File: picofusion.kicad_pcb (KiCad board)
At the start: 4 copper layers, 25.5 x 25.5 mm, 102 parts, among them J1 NORTH, J2 EAST, J3 WEST, J4 SOUTH, U1 W25Q16, U2 RP2040, U3 TLV71333PDQN, U4 ICM42605, U5 MMC5983MA, U6 ICP20100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

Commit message: draft: schematic and layout for H20R1
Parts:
- removed C13, C15, C24, C26: 0.1uF, Capacitor_SMD:C_0201_0603Metric
- removed C25: 1uF, Capacitor_SMD:C_0201_0603Metric
- removed R2, R3: 27, Resistor_SMD:R_0201_0603Metric
- removed R4, R5: 10K, Resistor_SMD:R_0402_1005Metric
- removed U2: RP2040, RP2040_minimal:RP2040-QFN-56
- C1: value 0.1uF -> 2u2
- C10: value 0.1uF -> 1u0
- C2, C4, C7, C9: value 0.1uF -> 0u1
- C3: value 1uF -> 0u1
- C6: value 0.1uF -> 4u7
- TP1: moved to F.Cu
- U1: value W25Q16 -> STM32F412CGUx; footprint USON:8-USON -> Package_DFN_QFN:QFN-48-1EP_7x7mm_P0.5mm_EP5.6x5.6mm
- moved C17 13.6 mm to (168.5, 39.2)
- moved C18 13.6 mm to (169.8, 37.6)
- moved C19 13.6 mm to (166.4, 39.2)
- moved U4 13.6 mm to (167.5, 37.1)
- moved C10 12.6 mm to (164.2, 50.0), turned to 180 degrees
- moved R14 12.6 mm to (158.6, 38.6), turned to -90 degrees
- moved C29 10.0 mm to (155.9, 40.8)
- moved C30 10.0 mm to (157.1, 39.5)
- moved U8 10.0 mm to (157.1, 40.8)
- moved C23 8.57 mm to (153.9, 36.9)
- moved C22 8.57 mm to (155.7, 38.7)
- moved U6 8.57 mm to (153.9, 38.7)
- moved R17 8.53 mm to (169.2, 45.4), turned to 180 degrees
- moved U1 7.93 mm to (163.0, 43.9)
- moved C1 7.65 mm to (168.0, 42.1), turned to 180 degrees
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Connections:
- C1 pad 1: +1V1 -> GND
- C1 pad 2: GND -> Net-(C1-Pad2)
- C11 pad 1: /RUN -> /nRST
- C2 pad 1: +1V1 -> +3V3
- C3 pad 1: +1V1 -> +3V3
- J1 pad 4: /I2C0_SCL -> /I2C1_SCL
- J1 pad 5: /I2C0_SDA -> /I2C1_SDA
- J2 pad 1: /SPI1_SCK_SD -> /SDIO_CMD
- J2 pad 2: /SPI1_POCI_SD -> /SDIO_D3
- J2 pad 3: /SPI1_PICO_SD -> /SDIO_D2
- J2 pad 4: /SPI1_nCS_SD -> /SDIO_D1
- J2 pad 5: /SD_nCD -> /SDIO_D0
- J2 pad 9: /RUN -> /nRST
- J4 pad 4: /UART0_TX_TELEM -> /UART2_TX_TELEM
- J4 pad 5: /UART0_RX_TELEM -> /UART2_RX_TELEM
- J4 pad 6: /UART0_CTS_TELEM -> /UART2_CTS_TELEM
- J4 pad 7: /UART0_RTS_TELEM -> /UART2_RTS_TELEM
- R1 pad 2: /RUN -> /nRST
- R12 pad 1: /PIO0_CAN_TX -> /CAN1_TX
- R13 pad 1: /PIO0_CAN_RX -> /CAN1_RX
- R18 pad 1: /RUN -> /nRST
- R8 pad 2: /I2C0_SCL -> /I2C1_SCL
- R9 pad 2: /I2C0_SDA -> /I2C1_SDA
- U1 pad 1: /QSPI_nCS -> +3V3
- U1 pad 2: /QSPI_SD1 -> unconnected-(U1-Pad2)
- U1 pad 3: /QSPI_SD2 -> /CAN_SILENT
- U1 pad 4: GND -> /IMU_HEATER
- U1 pad 5: /QSPI_SD0 -> /XIN
- U1 pad 6: /QSPI_SCK -> /XOUT
- U1 pad 7: /QSPI_SD3 -> /nRST
- U1 pad 8: +3V3 -> GND
- U5 pad 1: /I2C0_SCL -> /I2C1_SCL
- U5 pad 16: /I2C0_SDA -> /I2C1_SDA
- U6 pad 2: /I2C0_SCL -> /I2C1_SCL
- U6 pad 4: /I2C0_SDA -> /I2C1_SDA
- U7 pad 1: /PIO0_CAN_TX -> /CAN1_TX
- U7 pad 4: /PIO0_CAN_RX -> /CAN1_RX
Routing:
- net +5V: track 49.8 -> 14.9 mm, vias 6 -> 3
- net /I2C0_SCL: track 32.3 -> 0.00 mm, vias 3 -> 0
- net /I2C0_SDA: track 30.6 -> 0.00 mm, vias 2 -> 0
- net /I2C1_SCL: track 0.00 -> 27.2 mm, vias 0 -> 3
- net /I2C1_SDA: track 0.00 -> 26.2 mm, vias 0 -> 2
- net /RESV1: track 23.2 -> 0.00 mm, vias 1 -> 0
- net /SDIO_D3: track 0.00 -> 23.0 mm, vias 0 -> 1
- net /QSPI_nCS: track 23.1 -> 2.66 mm, vias 2 -> 0
- net /SDIO_D0: track 0.00 -> 20.3 mm, vias 0 -> 1
- net /SDIO_CMD: track 0.00 -> 18.2 mm
- net /BOOTSEL: track 3.94 -> 21.2 mm, vias 0 -> 4
- net +1V1: track 16.3 -> 0.00 mm, vias 2 -> 0
- net Net-(D4-Pad3): track 23.3 -> 7.92 mm, vias 4 -> 2
- net /SPI0_POCI: track 20.2 -> 5.32 mm
- net /UART0_TX_TELEM: track 14.7 -> 0.00 mm
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
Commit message: h20r1: more updates
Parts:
- moved C5 4.13 mm to (154.9, 49.1)
- moved C8 3.23 mm to (159.7, 50.6), turned to 0 degrees
- moved C2 2.68 mm to (157.9, 47.4), turned to 180 degrees
- moved G*** 2.29 mm to (162.7, 32.5)
- moved Y1 1.34 mm to (157.1, 49.9), turned to -90 degrees
- moved C10 0.68 mm to (163.6, 49.8)
- moved C9 0.68 mm to (163.6, 49.0)
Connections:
- U1 pad 2: unconnected-(U1-Pad2) -> /CAN_SILENT
- U1 pad 3: /CAN_SILENT -> /IMU_HEATER
- U1 pad 4: /IMU_HEATER -> unconnected-(U1-Pad4)
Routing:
- net /I2C1_SCL: track 27.2 -> 30.4 mm, vias 3 -> 2
- net /XOUT: track 9.60 -> 6.86 mm
- net /XIN: track 7.00 -> 9.71 mm
- net /UART2_RTS_TELEM: track 8.00 -> 6.62 mm, vias 1 -> 0
- net +3V3: track 33.5 -> 34.7 mm, vias 24 -> 23
- net /BOOTSEL: track 21.2 -> 20.1 mm, vias 4 -> 2
- net /CAN_SILENT: track 13.1 -> 12.2 mm, vias 2 -> 0
- net /IMU_HEATER: track 13.1 -> 12.3 mm
- net GND: track 36.1 -> 36.9 mm, vias 42 -> 43
- net /nRST: track 11.3 -> 11.9 mm, vias 2 -> 4
- net /UART2_RX_TELEM: track 13.0 -> 12.8 mm, vias 0 -> 1
- net /UART2_TX_TELEM: track 13.3 -> 13.4 mm, vias 0 -> 1
- net /UART2_CTS_TELEM: track 8.04 -> 8.12 mm, vias 1 -> 0

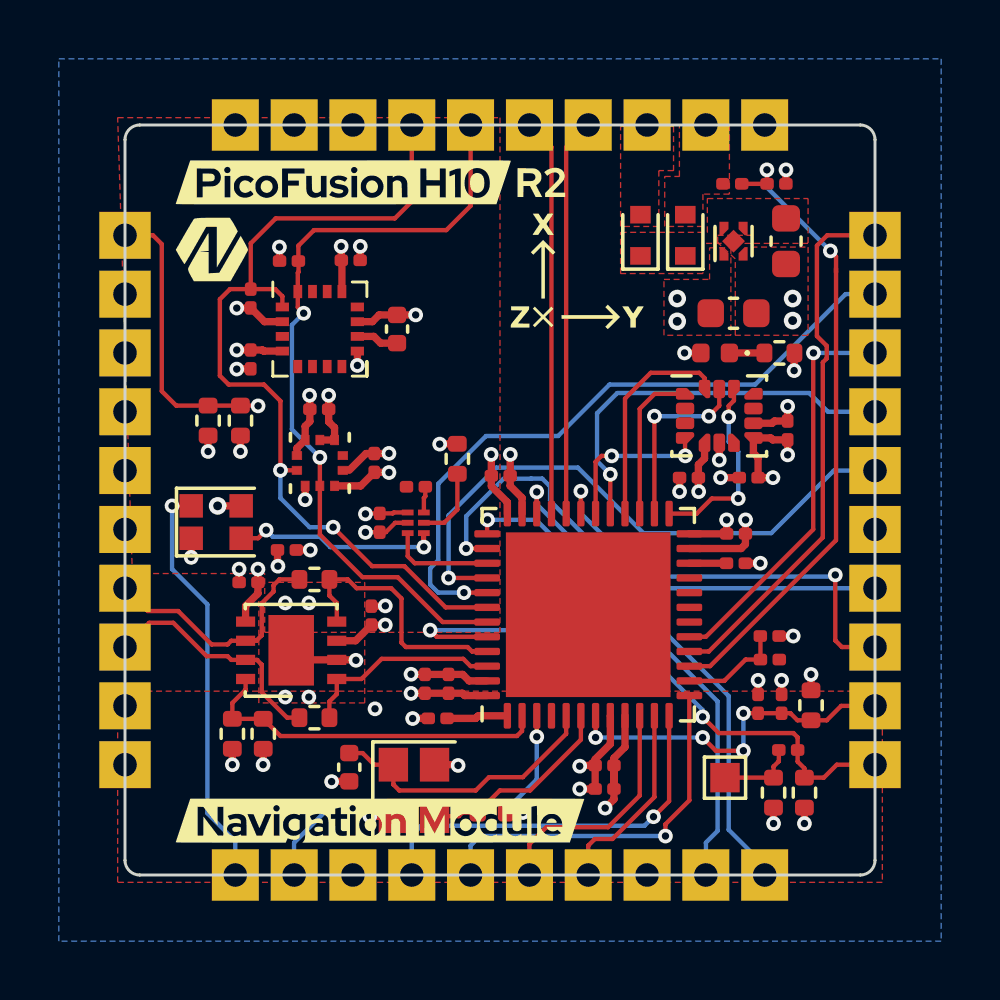
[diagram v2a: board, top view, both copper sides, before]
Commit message: replace sdio with spi2, finish routing, front silkscreen
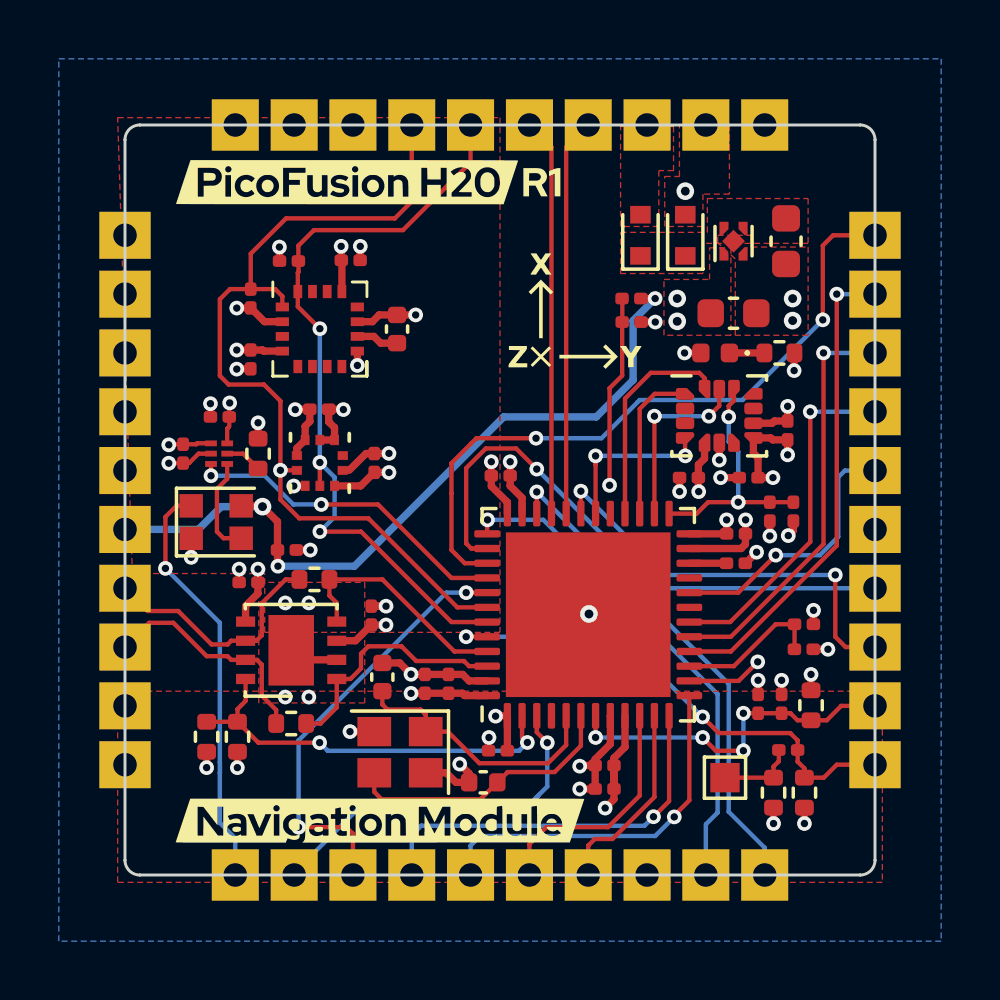
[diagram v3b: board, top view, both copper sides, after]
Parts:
- removed the G*** at (154.7, 29.2)
- removed the G*** at (150.2, 31.5)
- removed the G*** at (170.5, 29.2)
- added G***: LOGO, picofusion_stamp:r1, F.Cu at (162.3, 29.2)
- added G***: LOGO, picofusion_stamp:picofusion-h20, F.Cu at (155.9, 29.2)
- R23, R7: footprint Resistor_SMD:R_0402_1005Metric -> Resistor_SMD:R_0201_0603Metric
- moved R23 19.3 mm to (169.2, 40.4)
- moved R7 19.1 mm to (170.0, 40.4)
- moved R15 16.0 mm to (170.3, 45.1), turned to 180 degrees
- moved R16 15.0 mm to (170.3, 44.2)
- moved R17 13.1 mm to (164.5, 33.1)
- moved R22 11.7 mm to (164.5, 34.0)
- moved U8 7.09 mm to (150.4, 38.4)
- moved C29 7.09 mm to (149.2, 38.4)
- moved C30 7.08 mm to (150.5, 37.2)
- moved R14 6.78 mm to (151.8, 38.4)
- moved C5 3.26 mm to (156.0, 46.0), turned to 90 degrees
- moved C2 2.33 mm to (159.9, 48.5)
- moved Y1 1.38 mm to (156.6, 48.6), turned to 180 degrees
- moved G*** 1.35 mm to (162.6, 33.9)
- moved C8 1.07 mm to (159.4, 49.6), turned to 180 degrees
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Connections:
- net /SDIO_D2 renamed /SPI1_PICO
- J1 pad 3: /RESV1 -> unconnected-(J1-Pin_3-Pad3)
- J2 pad 1: /SDIO_CMD -> /SPI1_SCK
- J2 pad 2: /SDIO_D3 -> /SPI1_POCI
- J2 pad 4: /SDIO_D1 -> /SPI1_nCS
- J2 pad 5: /SDIO_D0 -> /RESV1
- J3 pad 1: /SPI0_nCS -> unconnected-(J3-Pin_1-Pad1)
- J3 pad 2: /SPI0_SCK -> unconnected-(J3-Pin_2-Pad2)
- J3 pad 3: /SPI0_PICO -> unconnected-(J3-Pin_3-Pad3)
- J3 pad 4: /SPI0_POCI -> unconnected-(J3-Pin_4-Pad4)
- J3 pad 5: /DRDY_ICM42605 -> unconnected-(J3-Pin_5-Pad5)
- U1 pad 16: /SDIO_CMD -> /SPI1_POCI
- U1 pad 18: /BUZZER -> /SPI1_nCS
- U1 pad 19: /RESV1 -> unconnected-(U1-PB1-Pad19)
- U1 pad 20: unconnected-(U1-Pad20) -> /RESV1
- U1 pad 29: /SDIO_D1 -> unconnected-(U1-PA8-Pad29)
- U1 pad 39: /NEOPIXEL_3V3 -> /SPI1_SCK
- U1 pad 40: /SDIO_D0 -> /NEOPIXEL_3V3
- U1 pad 41: /SDIO_D3 -> /BUZZER
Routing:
- net +5V: track 14.9 -> 41.9 mm, vias 3 -> 6
- net /SPI1_SCK: track 0.00 -> 23.4 mm, vias 0 -> 2
- net /SDIO_D3: track 23.0 -> 0.00 mm, vias 1 -> 0
- net /SDIO_D0: track 20.3 -> 0.00 mm, vias 1 -> 0
- net /SDIO_CMD: track 18.3 -> 0.00 mm
- net /3V3_SENSE: track 21.8 -> 5.02 mm, vias 2 -> 0
- net /SPI1_POCI: track 0.00 -> 16.3 mm, vias 0 -> 1
- net /BUZZER: track 0.00 -> 14.7 mm, vias 0 -> 2
- net /5V_SENSE: track 3.52 -> 17.2 mm, vias 0 -> 2
- net /SDIO_D1: track 13.5 -> 0.00 mm, vias 1 -> 0
- net /SPI1_nCS: track 0.00 -> 11.8 mm, vias 0 -> 1
- net /RESV1: track 0.00 -> 9.14 mm, vias 0 -> 1
- net /SPI0_nCS: track 16.3 -> 8.44 mm, vias 3 -> 2
- net /NEOPIXEL_3V3: track 3.59 -> 11.2 mm, vias 0 -> 2
- net Net-(D4-DIN): track 7.92 -> 3.36 mm, vias 2 -> 0
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
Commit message: cleanup and review of PicoFusion H20 R1
* update to KiCad 7
* add thermal vias to STM32F412CG QFN footprint
* update silkscreen branding
* update applicable silkscreen to Kicad 7 native text
* fix UART GNSS TX/RX swapped
* minor routing changes and cleanup
* replace DNP jump resistors with unpopulated test point footprint
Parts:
- removed the G*** at (169.8, 41.0)
- removed the G*** at (161.0, 50.2)
- removed the G*** at (163.0, 30.3)
- removed the G*** at (158.6, 36.8)
- removed the G*** at (162.6, 38.1)
- removed the G*** at (169.7, 43.0)
- removed the G*** at (160.0, 33.6)
- removed the G*** at (161.0, 30.4)
- removed the G*** at (161.0, 35.5)
- removed the G*** at (159.0, 50.9)
- removed the G*** at (167.0, 30.2)
- removed the G*** at (150.2, 41.0)
- removed the G*** at (169.0, 30.2)
- removed the G*** at (165.0, 30.2)
- removed the G*** at (163.0, 50.3)
- removed the G*** at (169.7, 45.0)
- removed the G*** at (157.0, 50.9)
- removed the G*** at (157.0, 44.7)
- removed the G*** at (150.3, 49.0)
- removed the G*** at (165.0, 49.8)
- removed the G*** at (169.7, 47.0)
- removed the G*** at (150.2, 47.0)
- R18, R19: footprint Resistor_SMD:R_0402_1005Metric -> TestPoint_Extra:TestPoint_2Pin_0402_1005Metric
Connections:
- net /BOOTSEL renamed /BOOT0
- net /QSPI_nCS renamed Net-(R20-Pad2)
- net /SPI0_PICO renamed /SPI2_PICO
- net /SPI0_POCI renamed /SPI2_POCI
- net /SPI0_SCK renamed /SPI2_SCK
- net /SPI0_nCS renamed /SPI2_nCS
- R19 pad 2: GND -> +3V3
- R21 pad 1: +3V3 -> GND
- U1 pad 31: /UART1_TX_GNSS -> /UART1_RX_GNSS
- U1 pad 38: /UART1_RX_GNSS -> /UART1_TX_GNSS
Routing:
- net /UART1_RX_GNSS: track 19.4 -> 12.1 mm
- net /UART1_TX_GNSS: track 14.1 -> 20.2 mm, vias 2 -> 1
- net +5V: track 41.9 -> 40.8 mm
- net GND: vias 41 -> 47
- net /I2C1_SCL: vias 1 -> 0
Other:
- board text added: "+3V3"
- board text added: "+5V"
- board text added: "Attitude & Heading Reference"
- board text added: "CTS"
- board text added: "GND"
- board text added: "Hobby Edition"
- board text added: "PicoFusion H20"
- board text added: "REV1"
- board text added: "RTS"
- board text added: "RX"
- board text added: "TX"
- board text added: "USB+"
- board text added: "USB-"

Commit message: update usb impedance/trace width, silkscreen
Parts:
- moved G*** 2.59 mm to (160.4, 32.6)
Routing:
- net /I2C1_SCL: track 30.3 -> 31.0 mm
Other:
- board text added: "BOOT"
- board text added: "PWR"
- board text added: "RST"
- board text added: "ST"

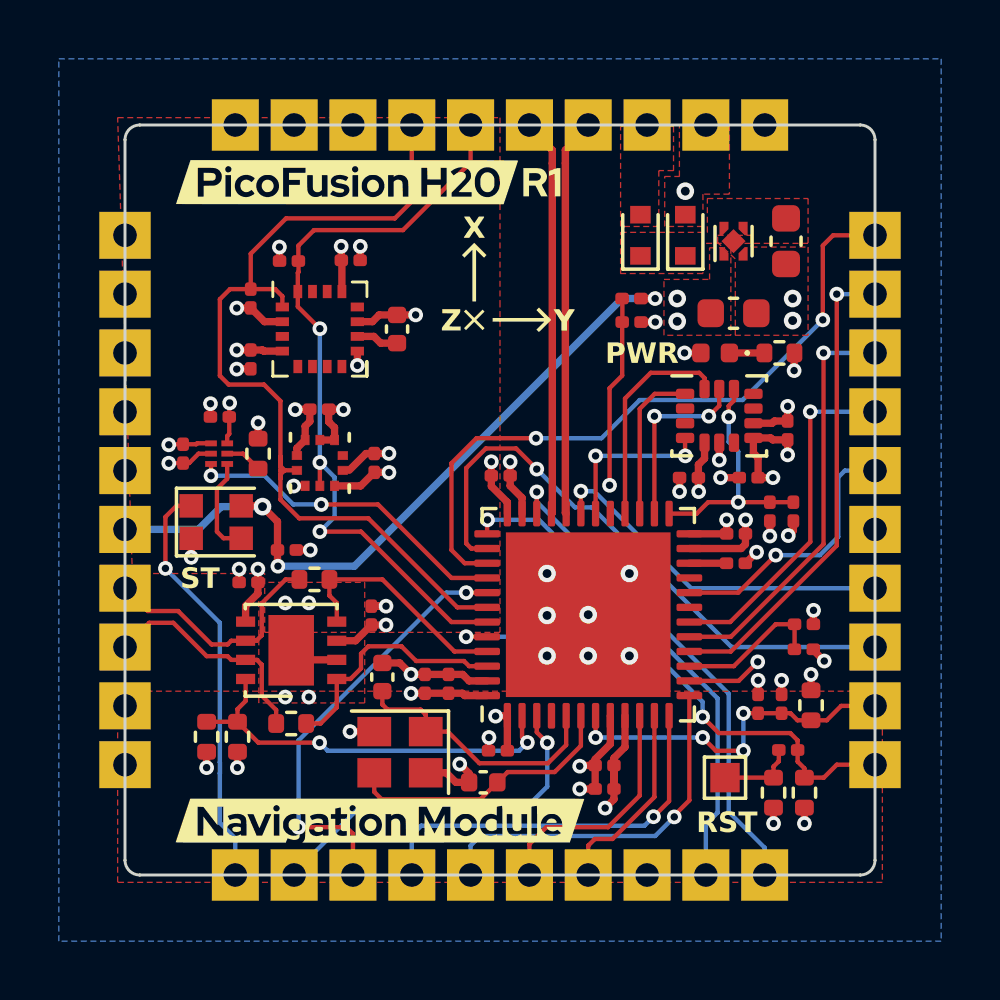
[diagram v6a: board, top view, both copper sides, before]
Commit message: update crystal
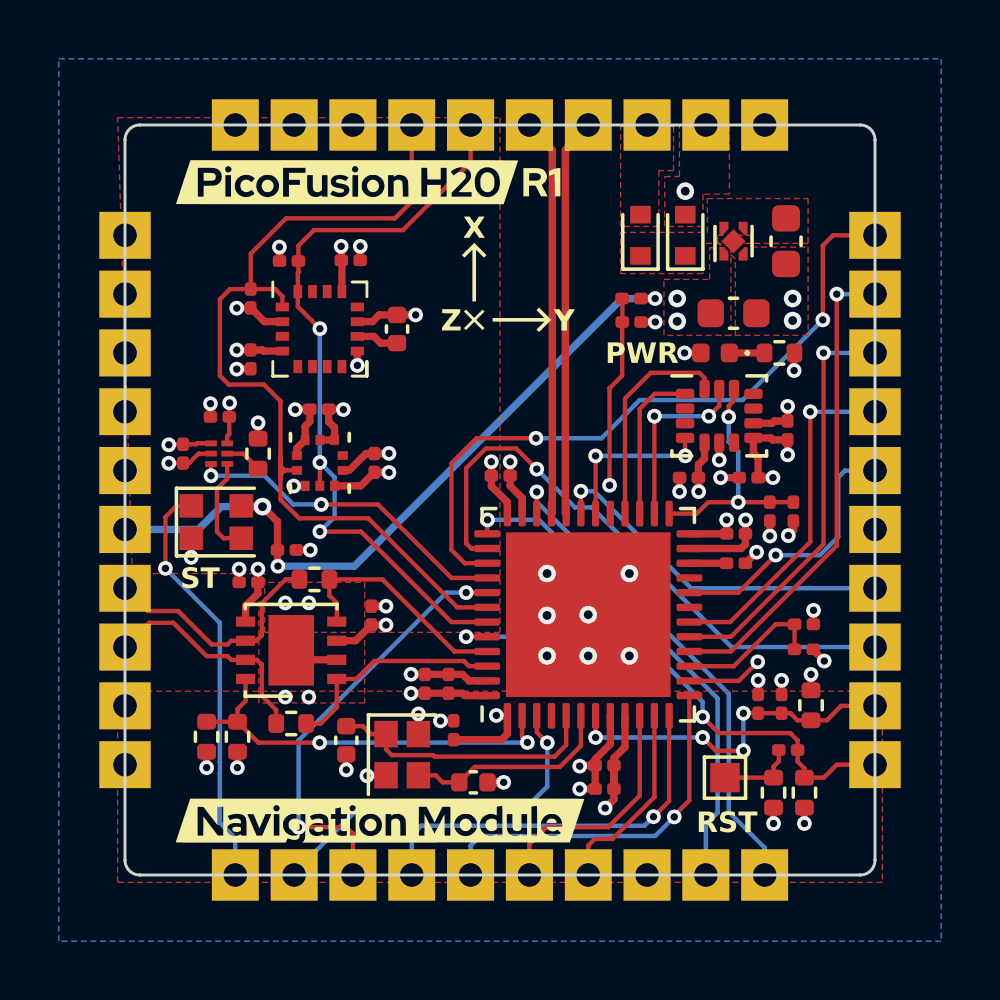
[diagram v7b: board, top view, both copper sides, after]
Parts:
- Y1: value 12MHz -> 16MHz; footprint Crystal:Crystal_SMD_2520-4Pin_2.5x2.0mm -> Crystal:Crystal_SMD_2016-4Pin_2.0x1.6mm
- moved C5 2.47 mm to (154.8, 48.2), turned to -90 degrees
- moved C2 1.66 mm to (158.4, 47.8), turned to 90 degrees
- moved C8 0.34 mm to (159.1, 49.6), turned to 0 degrees
- moved Y1 0.11 mm to (156.7, 48.7), turned to -90 degrees
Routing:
- net /XOUT: track 9.55 -> 7.16 mm
- net GND: track 38.0 -> 36.1 mm, vias 47 -> 49
- net +3V3: track 34.4 -> 35.7 mm
- net /CAN1_TX: track 8.38 -> 7.67 mm
